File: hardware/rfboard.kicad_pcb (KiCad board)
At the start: 2 copper layers, 30 x 36 mm, 20 parts, among them J1 10118194-0001LF, J2 CONN_01X11, J3 CONN_01X11, P2 CONN_01X03, P3 CONN_01X04, P5 CONN_01X01, U1 SAMD21E18, U2 RFM69CW-915MHZ, U3 MIC5504-3.3YM5-T5

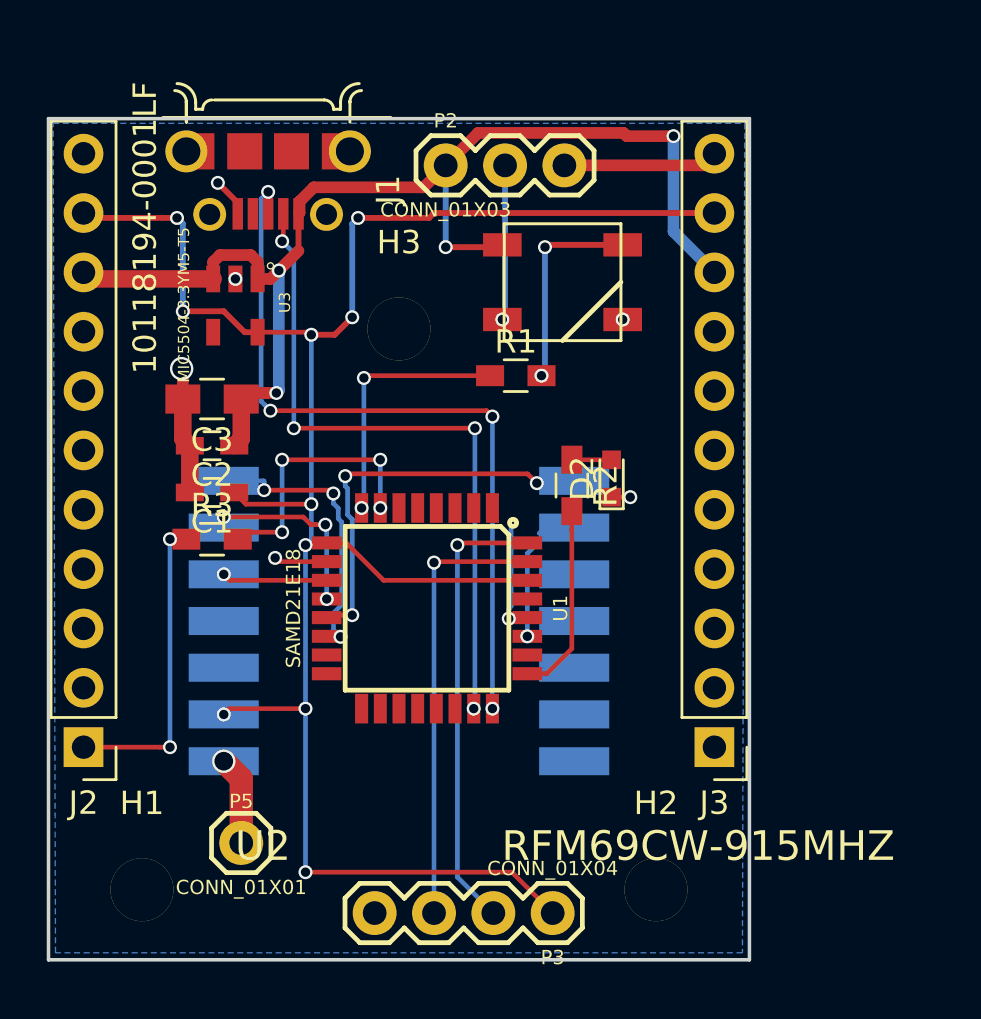
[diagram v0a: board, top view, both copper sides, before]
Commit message: Move right header to match breadboard spacing (2.54mm pitch)
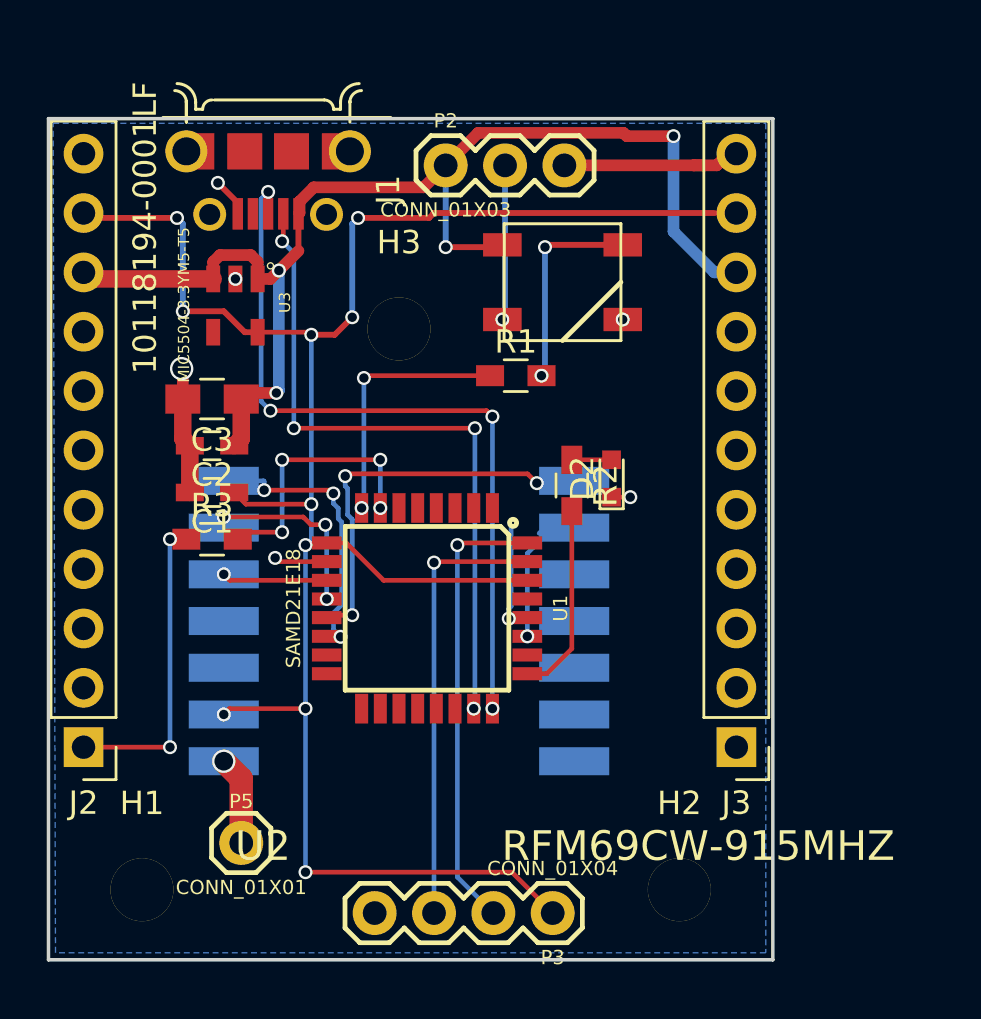
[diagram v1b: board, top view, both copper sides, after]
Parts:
- moved H2 1.00 mm to (133.0, 161.0)
- moved J3 0.94 mm to (135.4, 154.9)
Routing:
- net GND: track 21.6 -> 22.9 mm
- net +5V: track 53.6 -> 54.5 mm
- net +3V3: track 87.6 -> 88.6 mm
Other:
- board size 30 x 36 mm -> 31 x 36 mm

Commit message: Finished layout.
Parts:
- moved D2 10.4 mm to (129.6, 153.8)
- moved R2 9.70 mm to (128.1, 153.4), turned to 90 degrees
- moved H1 1.50 mm to (110.0, 159.5)
- moved H2 1.50 mm to (133.0, 159.5)
- moved R1 1.43 mm to (127.3, 138.4)
- moved P3 1.00 mm to (127.5, 161.0)
- moved P5 0.35 mm to (114.6, 159.0)
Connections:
- J2 pad 2: Net-(J2-Pad2) -> L1
- J2 pad 3: Net-(J2-Pad3) -> L2
- J2 pad 4: Net-(J2-Pad4) -> L3
- J2 pad 5: Net-(J2-Pad5) -> L4
- J2 pad 6: Net-(J2-Pad6) -> L5
- J2 pad 7: Net-(J2-Pad7) -> L6
- J2 pad 8: Net-(J2-Pad8) -> +5V
- J3 pad 1: Net-(J3-Pad1) -> R1
- J3 pad 2: Net-(J3-Pad2) -> R2
- J3 pad 3: Net-(J3-Pad3) -> R3
- J3 pad 4: Net-(J3-Pad4) -> R4
- J3 pad 5: Net-(J3-Pad5) -> R5
- J3 pad 6: Net-(J3-Pad6) -> R6
- J3 pad 7: Net-(J3-Pad7) -> R7
- J3 pad 8: Net-(J3-Pad8) -> R8
- U1 pad 1: Net-(U1-Pad1) -> R3
- U1 pad 15: Net-(U1-Pad15) -> L6
- U1 pad 16: Net-(U1-Pad16) -> L5
- U1 pad 17: Net-(U1-Pad17) -> L4
- U1 pad 18: Net-(U1-Pad18) -> L3
- U1 pad 19: Net-(U1-Pad19) -> L2
- U1 pad 2: Net-(U1-Pad2) -> R4
- U1 pad 20: Net-(U1-Pad20) -> L1
- U1 pad 21: Net-(U1-Pad21) -> R1
- U1 pad 22: Net-(U1-Pad22) -> R2
- U1 pad 3: Net-(U1-Pad3) -> R5
- U1 pad 4: Net-(U1-Pad4) -> R6
- U1 pad 5: Net-(U1-Pad5) -> R7
- U1 pad 6: Net-(U1-Pad6) -> R8
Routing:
- net R8: track 0.00 -> 19.9 mm, vias 0 -> 2
- net L6: track 0.00 -> 19.2 mm
- net R5: track 0.00 -> 17.7 mm, vias 0 -> 2
- net R6: track 0.00 -> 17.3 mm, vias 0 -> 2
- net L5: track 0.00 -> 17.3 mm
- net L4: track 0.00 -> 17.2 mm
- net L3: track 0.00 -> 17.2 mm
- net R7: track 0.00 -> 16.8 mm, vias 0 -> 2
- net L1: track 0.00 -> 16.6 mm
- net L2: track 0.00 -> 16.5 mm
- net R1: track 0.00 -> 15.5 mm
- net R2: track 0.00 -> 15.3 mm
- net R4: track 0.00 -> 13.6 mm
- net R3: track 0.00 -> 12.6 mm
- net SIMPLE_LED: track 8.24 -> 1.83 mm
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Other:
- board size 31 x 36 mm -> 31 x 34.6 mm
- net class Default: clearance 0.2 -> 0.1999
- rule trace_clearance: 0.2 -> 0.1999

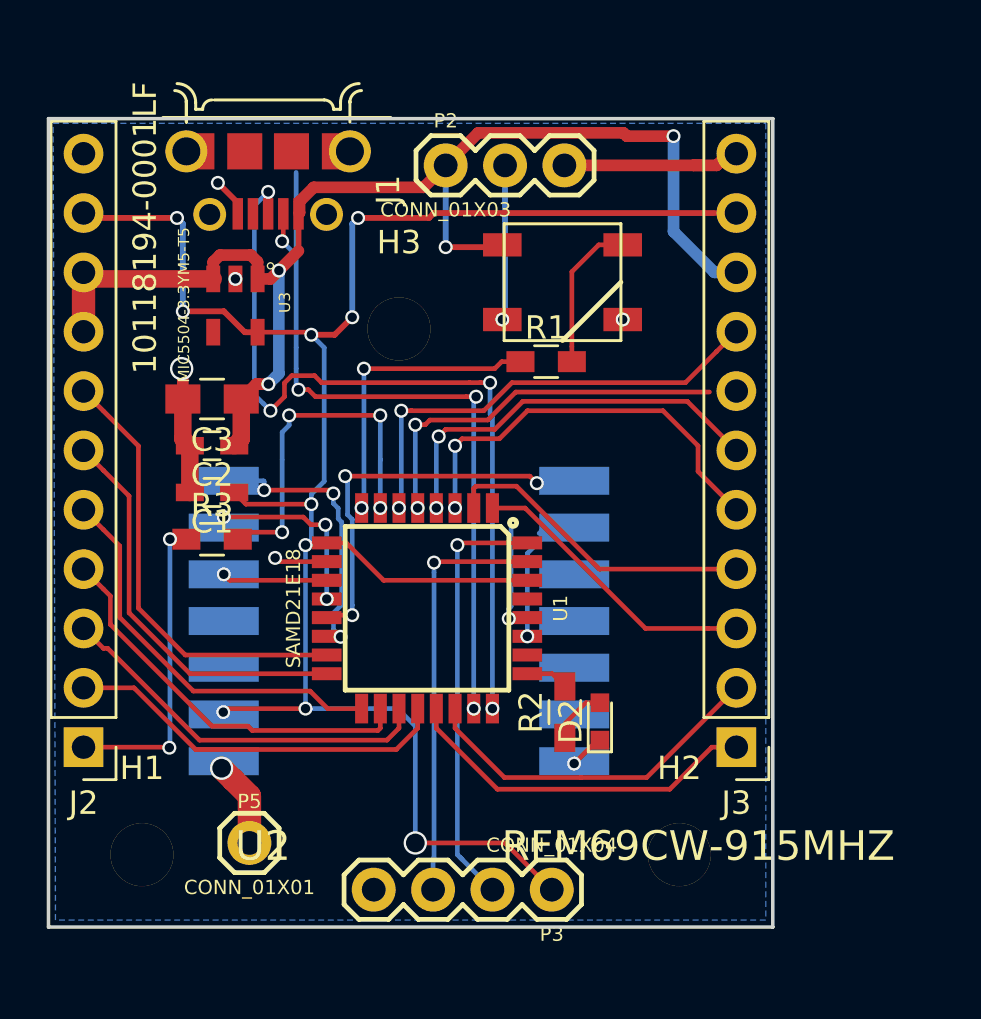
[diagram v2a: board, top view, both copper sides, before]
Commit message: Optimized ground plane
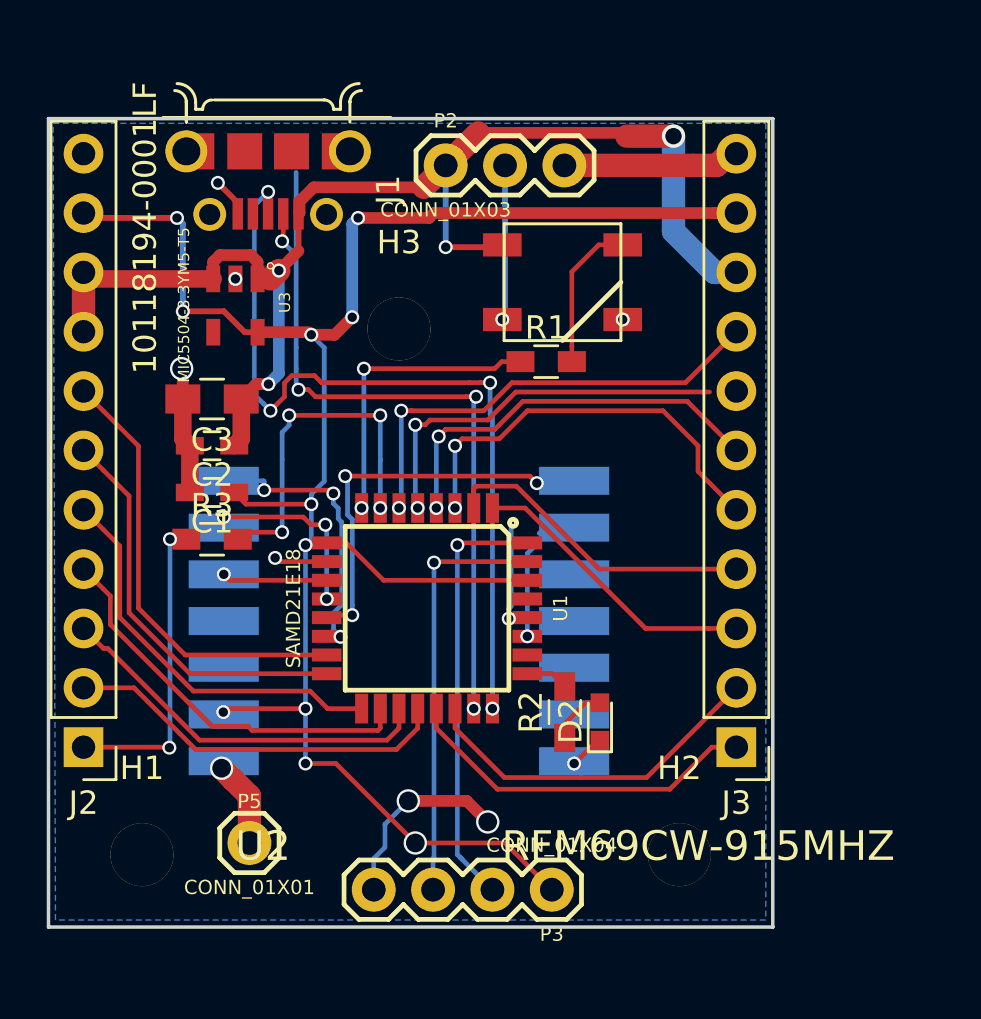
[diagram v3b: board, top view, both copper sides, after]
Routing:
- net GND: track 23.8 -> 31.6 mm, vias 7 -> 9
- net +3V3: track 87.4 -> 85.8 mm, vias 10 -> 11

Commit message: Make board narrower
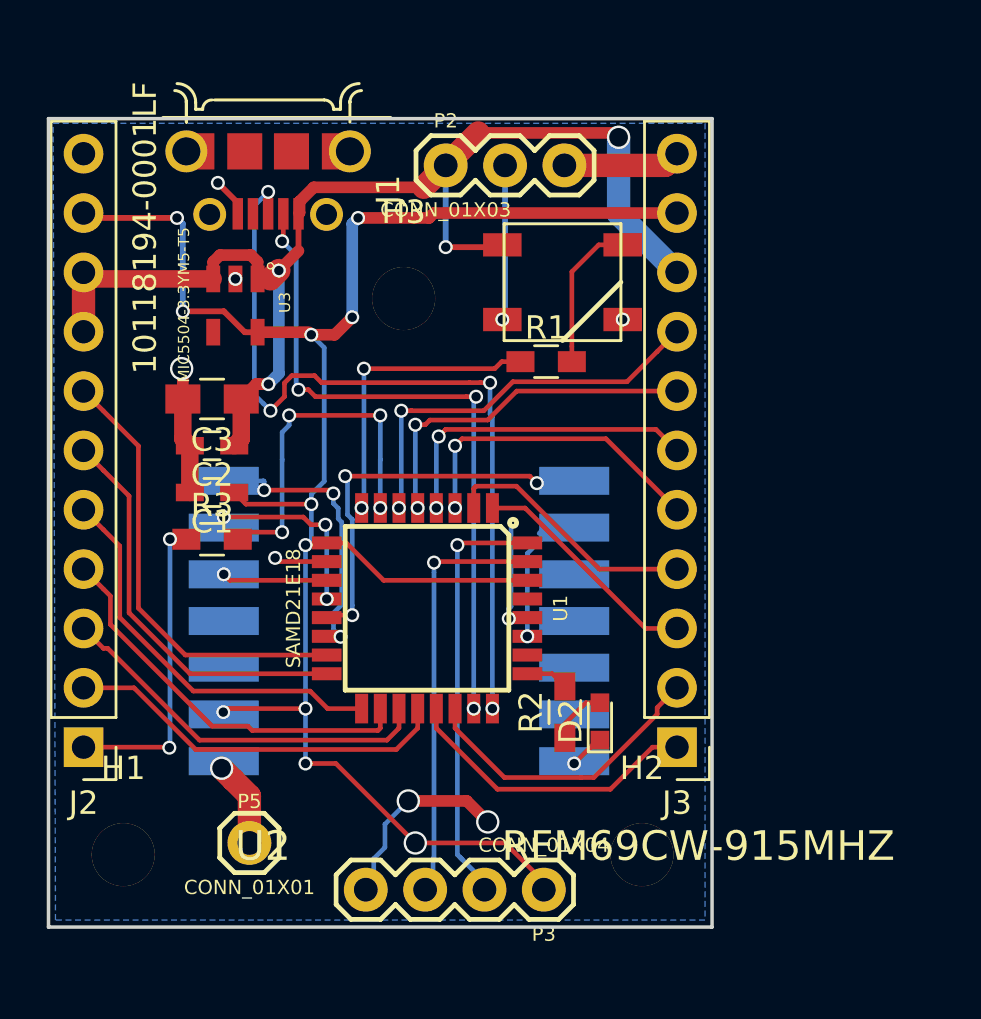
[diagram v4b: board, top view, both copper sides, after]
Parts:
- moved J3 2.54 mm to (132.9, 154.9)
- moved H2 1.60 mm to (131.4, 159.5)
- moved H3 1.32 mm to (121.2, 135.7)
- moved H1 0.80 mm to (109.2, 159.5)
- moved P3 0.34 mm to (127.2, 161.0)
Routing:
- net R5: track 17.7 -> 13.5 mm
- net R6: track 17.3 -> 13.8 mm
- net USB_D-: track 32.4 -> 29.0 mm
- net +5V: track 56.7 -> 53.7 mm
- net +3V3: track 85.8 -> 83.3 mm
- net R8: track 19.9 -> 17.4 mm
- net R4: track 13.6 -> 11.0 mm
- net R3: track 12.6 -> 10.0 mm
- net R1: track 15.5 -> 13.0 mm
- net GND: track 31.6 -> 29.1 mm
- net R2: track 15.3 -> 13.0 mm
- net R7: track 16.8 -> 15.4 mm
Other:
- board size 31 x 34.6 mm -> 28.4 x 34.6 mm
- net class Default: clearance 0.1999 -> 0.199
- rule trace_clearance: 0.1999 -> 0.199

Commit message: Add silkscreen
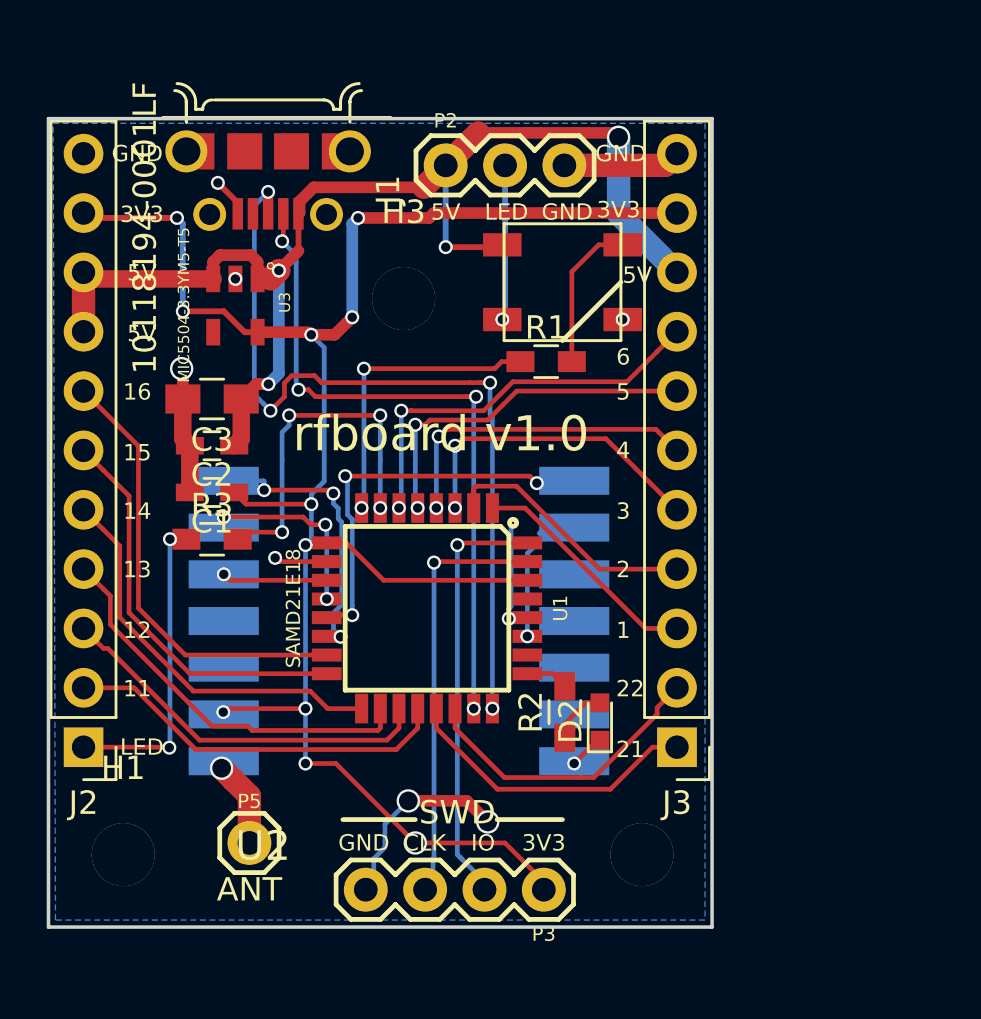
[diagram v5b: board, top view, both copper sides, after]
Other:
- board text added: "1"
- board text added: "11"
- board text added: "12"
- board text added: "13"
- board text added: "14"
- board text added: "15"
- board text added: "16"
- board text added: "2"
- board text added: "21"
- board text added: "22"
- board text added: "3"
- board text added: "3V3"
- board text added: "4"
- board text added: "5"
- board text added: "5V"
- board text added: "6"
- board text added: "ANT"
- board text added: "CLK"
- board text added: "GND"
- board text added: "IO"
- board text added: "LED"
- board text added: "SWD"
- board text added: "TEST"
- board text added: "rfboard v1.0"
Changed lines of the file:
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@@
     (links 61)
     (no_connects 0)
-    (area 105.924999 127.924999 137.075001 162.675001)
+    (area 105.924999 127.924999 134.475001 162.675001)
     (thickness 1.6)
-    (drawings 4)
+    (drawings 40)
     (tracks 372)
     (zones 0)
@@
     (47 F.CrtYd user)
     (48 B.Fab user)
-    (49 F.Fab user)
+    (49 F.Fab user hide)
   )
   (setup
@@
       (effects (font (size 1.27 1.27) (thickness 0.1016)))
     )
-    (fp_text value RFM69CW-915MHZ (at 12.80922 9.63422) (layer F.SilkS)
+    (fp_text value RFM69CW-915MHZ (at 12.80922 9.63422) (layer F.SilkS) hide
       (effects (font (size 1.27 1.27) (thickness 0.1016)))
     )
@@
       (effects (font (size 1 1) (thickness 0.15)))
     )
-    (fp_text value LED (at 0 1.35 90) (layer F.Fab)
+    (fp_text value LED (at 0 1.35 90) (layer F.Fab) hide
       (effects (font (size 1 1) (thickness 0.15)))
     )
@@
       (effects (font (size 0.6096 0.6096) (thickness 0.127)))
     )
-    (fp_text value CONN_01X03 (at 0 1.905) (layer F.SilkS)
+    (fp_text value CONN_01X03 (at 0 1.905) (layer F.SilkS) hide
       (effects (font (size 0.6096 0.6096) (thickness 0.127)))
     )
@@
       (effects (font (size 0.6096 0.6096) (thickness 0.127)))
     )
-    (fp_text value CONN_01X04 (at 0 1.905 180) (layer F.SilkS)
+    (fp_text value CONN_01X04 (at 0 1.905 180) (layer F.SilkS) hide
       (effects (font (size 0.6096 0.6096) (thickness 0.127)))
     )
@@
       (effects (font (size 0.6096 0.6096) (thickness 0.127)))
     )
-    (fp_text value CONN_01X01 (at 0 1.905) (layer F.SilkS)
+    (fp_text value CONN_01X01 (at 0.2 2.9) (layer F.SilkS) hide
       (effects (font (size 0.6096 0.6096) (thickness 0.127)))
     )
@@
     (descr "Mounting Hole 2.7mm, M2.5")
     (tags "mounting hole 2.7mm m2.5")
-    (fp_text reference H2 (at 0 -3.7) (layer F.SilkS)
+    (fp_text reference H2 (at 0 -3.7) (layer F.SilkS) hide
       (effects (font (size 1 1) (thickness 0.15)))
     )
@@
     (pad 1 thru_hole circle (at 0 0) (size 2.7 2.7) (drill 2.7) (layers *.Cu *.Mask))
   )
+  (gr_circle (center 114 137.4) (end 114.7 137.4) (layer B.SilkS) (width 1.5))
+  (gr_text TEST (at 113.8 134.5) (layer B.SilkS)
+    (effects (font (size 1.5 1.5) (thickness 0.3)) (justify mirror))
+  )
+  (gr_text "rfboard v1.0" (at 122.8 141.5) (layer F.SilkS)
+    (effects (font (size 1.5 1.5) (thickness 0.3)))
+  )
+  (gr_text 21 (at 130.9 155) (layer F.SilkS)
+    (effects (font (size 0.7 0.7) (thickness 0.15)))
+  )
+  (gr_text 22 (at 130.9 152.4) (layer F.SilkS)
+    (effects (font (size 0.7 0.7) (thickness 0.15)))
+  )
+  (gr_text 6 (at 130.6 138.2) (layer F.SilkS)
+    (effects (font (size 0.7 0.7) (thickness 0.15)))
+  )
+  (gr_text 5 (at 130.6 139.7) (layer F.SilkS)
+    (effects (font (size 0.7 0.7) (thickness 0.15)))
+  )
+  (gr_text 4 (at 130.6 142.2) (layer F.SilkS)
+    (effects (font (size 0.7 0.7) (thickness 0.15)))
+  )
+  (gr_text 3 (at 130.6 144.8) (layer F.SilkS)
+    (effects (font (size 0.7 0.7) (thickness 0.15)))
+  )
+  (gr_text 2 (at 130.6 147.3) (layer F.SilkS)
+    (effects (font (size 0.7 0.7) (thickness 0.15)))
+  )
+  (gr_text 1 (at 130.6 149.9) (layer F.SilkS)
+    (effects (font (size 0.7 0.7) (thickness 0.15)))
+  )
+  (gr_text 11 (at 109.8 152.4) (layer F.SilkS)
+    (effects (font (size 0.7 0.7) (thickness 0.15)))
+  )
+  (gr_text 12 (at 109.8 149.9) (layer F.SilkS)
+    (effects (font (size 0.7 0.7) (thickness 0.15)))
+  )
+  (gr_text 13 (at 109.8 147.3) (layer F.SilkS)
+    (effects (font (size 0.7 0.7) (thickness 0.15)))
+  )
+  (gr_text 14 (at 109.8 144.8) (layer F.SilkS)
+    (effects (font (size 0.7 0.7) (thickness 0.15)))
+  )
+  (gr_text 15 (at 109.8 142.3) (layer F.SilkS)
+    (effects (font (size 0.7 0.7) (thickness 0.15)))
+  )
+  (gr_text 16 (at 109.8 139.7) (layer F.SilkS)
+    (effects (font (size 0.7 0.7) (thickness 0.15)))
+  )
+  (gr_text 5V (at 123 132) (layer F.SilkS)
+    (effects (font (size 0.7 0.7) (thickness 0.15)))
+  )
+  (gr_text LED (at 125.6 132) (layer F.SilkS)
+    (effects (font (size 0.7 0.7) (thickness 0.15)))
+  )
+  (gr_text GND (at 128.2 132) (layer F.SilkS)
+    (effects (font (size 0.7 0.7) (thickness 0.15)))
+  )
+  (gr_line (start 125.2 158) (end 128 158) (layer F.SilkS) (width 0.2))
+  (gr_line (start 121.7 158) (end 118.6 158) (layer F.SilkS) (width 0.2))
+  (gr_text SWD (at 123.5 157.7) (layer F.SilkS)
+    (effects (font (size 1 1) (thickness 0.2)))
+  )
+  (gr_text 3V3 (at 127.2 159) (layer F.SilkS)
+    (effects (font (size 0.7 0.7) (thickness 0.15)))
+  )
+  (gr_text IO (at 124.6 159) (layer F.SilkS)
+    (effects (font (size 0.7 0.7) (thickness 0.15)))
+  )
+  (gr_text CLK (at 122.1 159) (layer F.SilkS)
+    (effects (font (size 0.7 0.7) (thickness 0.15)))
+  )
+  (gr_text GND (at 119.5 159) (layer F.SilkS)
+    (effects (font (size 0.7 0.7) (thickness 0.15)))
+  )
+  (gr_text ANT (at 114.6 161) (layer F.SilkS)
+    (effects (font (size 1 1) (thickness 0.2)))
+  )
+  (gr_text LED (at 110 154.9) (layer F.SilkS)
+    (effects (font (size 0.7 0.7) (thickness 0.15)))
+  )
+  (gr_text 5V (at 110 137.2) (layer F.SilkS)
+    (effects (font (size 0.7 0.7) (thickness 0.15)))
+  )
+  (gr_text 5V (at 110 134.6) (layer F.SilkS)
+    (effects (font (size 0.7 0.7) (thickness 0.15)))
+  )
+  (gr_text 3V3 (at 110 132.1) (layer F.SilkS)
+    (effects (font (size 0.7 0.7) (thickness 0.15)))
+  )
+  (gr_text GND (at 109.8 129.5) (layer F.SilkS)
+    (effects (font (size 0.7 0.7) (thickness 0.15)))
+  )
+  (gr_text 5V (at 131.2 134.7) (layer F.SilkS)
+    (effects (font (size 0.7 0.7) (thickness 0.15)))
+  )
+  (gr_text 3V3 (at 130.4 131.9) (layer F.SilkS)
+    (effects (font (size 0.7 0.7) (thickness 0.15)))
+  )
+  (gr_text GND (at 130.5 129.5) (layer F.SilkS)
+    (effects (font (size 0.7 0.7) (thickness 0.15)))
+  )
   (gr_line (start 106 162.6) (end 106 128) (layer Edge.Cuts) (width 0.15))
